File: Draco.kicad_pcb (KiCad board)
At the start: 2 copper layers, 114.3 x 44.5 mm, 122 parts, among them J1 Conn_01x03, J10 Conn_01x03, J11 Conn_01x06, J12 Conn_02x05_Odd_Even, J13 Conn_01x04, J14 Conn_01x01, J15 Micro_SD_Card, J16 Conn_01x03, J17 CHARGE_A, J18 CHARGE_C, J19 CHARGE_B, J2 Conn_01x03, J20 Conn_01x04, J3 Conn_01x03, J4 Conn_01x03, J5 Conn_01x03, J6 Conn_01x03, J7 Conn_01x03, J8 Conn_01x03, J9 Conn_01x03, Q1 BC817, Q2 Q_NMOS_DGS, Q3 BC817, Q4 Q_NMOS_DGS, Q5 BC817, Q6 Q_NMOS_DGS, U1 ATMEGA2560-16AU, U2 LOGIC-TXS0108EPWR(TSSOP20), U3 RFM95HW, U4 TPS54332, U5 TLV62568, U6 SAM-M8Q, U7 LSM9DS1TR‎, U8 MS5607, Y1 16MHz

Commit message: Added dragon
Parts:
- added G***: LOGO, Current_Control_Systems:Draco_Logo, B.Cu at (137.5, 98.3)
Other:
- board text added: "CHARGE_A"
- board text added: "CHARGE_B"
- board text added: "CHARGE_C"
- board text added: "VIN 8.4V"

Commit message: Starting design review
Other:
- board text added: "5V"
- board text added: "CAM"
- board text added: "CPU PWR"
- board text added: "DTR"
- board text added: "GND"
- board text added: "ISP"
- board text added: "MISO"
- board text added: "MOSI"
- board text added: "NC"
- board text added: "RX"
- board text added: "SERVO PWR"
- board text added: "TEST_STAND"
- board text added: "TX"
- board text added: "VIN"
- board text added: "VIN 6-22V"
- board text added: "~~ + -"
- board text removed: "VIN 8.4V"
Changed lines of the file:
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@@
     (links 323)
     (no_connects 4)
-    (area 76.124999 76.124999 190.575001 120.725001)
+    (area 67.524143 73.53518 199.252058 122.996953)
     (thickness 1.6)
-    (drawings 10)
+    (drawings 37)
     (tracks 1618)
     (zones 0)
@@
   (page A4)
   (layers
-    (0 F.Cu signal hide)
-    (31 B.Cu signal hide)
+    (0 F.Cu signal)
+    (31 B.Cu signal)
     (32 B.Adhes user)
     (33 F.Adhes user)
@@
     (41 Cmts.User user)
     (42 Eco1.User user)
-    (43 Eco2.User user hide)
+    (43 Eco2.User user)
     (44 Edge.Cuts user)
     (45 Margin user)
@@
   )
   (setup
-    (last_trace_width 0.16)
+    (last_trace_width 0.25)
     (user_trace_width 0.16)
     (user_trace_width 0.75)
@@
     (pad_to_mask_clearance 0.2)
     (aux_axis_origin 0 0)
-    (visible_elements 7FFFEDFF)
+    (visible_elements 7FFFEFFF)
     (pcbplotparams
       (layerselection 0x00030_80000001)
@@
     (descr "Through hole straight pin header, 1x03, 2.54mm pitch, single row")
     (tags "Through hole pin header THT 1x03 2.54mm single row")
-    (fp_text reference JP1 (at 0.0508 7.2644 180) (layer F.SilkS)
+    (fp_text reference JP1 (at 0.0508 7.2644) (layer F.SilkS) hide
       (effects (font (size 1 1) (thickness 0.15)))
     )
@@
     (descr "Through hole straight pin header, 1x02, 2.54mm pitch, single row")
     (tags "Through hole pin header THT 1x02 2.54mm single row")
-    (fp_text reference JP2 (at 0.0254 -2.1844) (layer F.SilkS)
+    (fp_text reference JP2 (at 0.0254 -2.1844) (layer F.SilkS) hide
       (effects (font (size 1 1) (thickness 0.15)))
     )
@@
       (xy -7.2136 3.7846)) (layer B.SilkS) (width 0.01))
   )
+  (gr_text TX (at 133.2738 79.9592) (layer F.SilkS)
+    (effects (font (size 0.5 0.5) (thickness 0.125)))
+  )
+  (gr_text RX (at 135.89 79.9338) (layer F.SilkS)
+    (effects (font (size 0.5 0.5) (thickness 0.125)))
+  )
+  (gr_text NC (at 141.0208 79.9592) (layer F.SilkS)
+    (effects (font (size 0.5 0.5) (thickness 0.125)))
+  )
+  (gr_text GND (at 143.5608 79.9846) (layer F.SilkS)
+    (effects (font (size 0.5 0.5) (thickness 0.125)))
+  )
+  (gr_text 5V (at 138.4554 79.9338) (layer F.SilkS)
+    (effects (font (size 0.5 0.5) (thickness 0.125)))
+  )
+  (gr_text DTR (at 130.7592 79.9592) (layer F.SilkS)
+    (effects (font (size 0.5 0.5) (thickness 0.125)))
+  )
+  (gr_line (start 108.9152 117.3226) (end 108.966 117.3226) (angle 90) (layer F.SilkS) (width 0.2))
+  (gr_line (start 108.9152 117.8814) (end 108.9152 117.3226) (angle 90) (layer F.SilkS) (width 0.2))
+  (gr_line (start 108.9152 111.2266) (end 108.9152 111.7346) (angle 90) (layer F.SilkS) (width 0.2))
+  (gr_line (start 108.9152 111.252) (end 109.1438 111.252) (angle 90) (layer F.SilkS) (width 0.2))
+  (gr_line (start 108.9152 114.2238) (end 109.093 114.2238) (angle 90) (layer F.SilkS) (width 0.2))
+  (gr_line (start 108.9152 113.7158) (end 108.9152 114.2238) (angle 90) (layer F.SilkS) (width 0.2))
+  (gr_line (start 108.9152 114.8842) (end 109.1184 114.8842) (angle 90) (layer F.SilkS) (width 0.2))
+  (gr_line (start 108.9152 115.3668) (end 108.9152 114.8842) (angle 90) (layer F.SilkS) (width 0.2))
+  (gr_line (start 108.9152 117.8814) (end 109.1184 117.8814) (angle 90) (layer F.SilkS) (width 0.2))
+  (gr_text 5V (at 108.8644 116.2812 90) (layer F.SilkS)
+    (effects (font (size 0.5 0.5) (thickness 0.125)))
+  )
+  (gr_text VIN (at 108.8898 112.6236 90) (layer F.SilkS)
+    (effects (font (size 0.5 0.5) (thickness 0.125)))
+  )
+  (gr_text "SERVO\nPWR" (at 110.744 119.4308) (layer F.SilkS)
+    (effects (font (size 0.5 0.5) (thickness 0.125)))
+  )
+  (gr_text "CPU\nPWR" (at 90.7796 102.2604) (layer F.SilkS)
+    (effects (font (size 1 1) (thickness 0.25)))
+  )
+  (gr_text ISP (at 118.4148 92.71) (layer F.SilkS)
+    (effects (font (size 1 1) (thickness 0.25)))
+  )
+  (gr_text GND (at 115.7478 77.4192) (layer F.SilkS)
+    (effects (font (size 0.5 0.5) (thickness 0.125)))
+  )
+  (gr_text "MISO\n" (at 121.2088 77.4446) (layer F.SilkS)
+    (effects (font (size 0.5 0.5) (thickness 0.125)))
+  )
+  (gr_text 5V (at 115.5954 91.3384) (layer F.SilkS)
+    (effects (font (size 0.5 0.5) (thickness 0.125)))
+  )
+  (gr_text MOSI (at 121.3104 91.313) (layer F.SilkS)
+    (effects (font (size 0.5 0.5) (thickness 0.125)))
+  )
+  (gr_text "~~ + -" (at 150.368 116.4844 270) (layer F.SilkS)
+    (effects (font (size 1.5 1.5) (thickness 0.3)))
+  )
+  (gr_text "CAM\n" (at 162.306 83.6168) (layer F.SilkS)
+    (effects (font (size 1 1) (thickness 0.25)))
+  )
+  (gr_text TEST_STAND (at 152.5016 83.6422) (layer F.SilkS)
+    (effects (font (size 1 1) (thickness 0.25)))
+  )
   (gr_text "CHARGE_B\n" (at 109.5248 76.962) (layer F.SilkS)
     (effects (font (size 1 1) (thickness 0.25)))
@@
     (effects (font (size 1 1) (thickness 0.25)))
   )
-  (gr_text "VIN 8.4V" (at 88.0618 110.8456 90) (layer F.SilkS)
+  (gr_text "VIN 6-22V" (at 88.0618 110.8456 90) (layer F.SilkS)
     (effects (font (size 0.5 0.5) (thickness 0.125)))
   )
@@
     (polygon
       (pts
-        (xy 76.2 120.6246) (xy 190.4746 120.6246) (xy 190.5 76.2) (xy 76.2 76.2254) (xy 76.2254 76.2254)
+        (xy 76.2 76.2254) (xy 76.2 120.6246) (xy 190.5254 120.65) (xy 190.4746 76.2254)
       )
     )

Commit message: Added camera resistor divider
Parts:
- added R38: 0, Resistors_SMD:R_0805, B.Cu at (164.3, 83.3)
- added R39: 0, Resistors_SMD:R_0805, B.Cu at (166.9, 83.3)
- added R40: 0, Resistors_SMD:R_0805, B.Cu at (169.3, 83.2)
- R2: value 1k -> 2k7
- R3: value 1k -> 4k7
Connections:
- net /~FIRE_A renamed /FIRE_A
- net /~FIRE_B renamed /FIRE_B
- net /~FIRE_C renamed /FIRE_C
- J11 pad 5: (no net) -> Net-(J11-Pad5)
- J12 pad 3: (no net) -> Net-(J12-Pad3)
- J15 pad 1: (no net) -> Net-(J15-Pad1)
- J15 pad 8: (no net) -> Net-(J15-Pad8)
- U1 pad 1: (no net) -> Net-(U1-Pad1)
- U1 pad 12: (no net) -> Net-(U1-Pad12)
- U1 pad 13: (no net) -> Net-(U1-Pad13)
- U1 pad 14: (no net) -> Net-(U1-Pad14)
- U1 pad 18: (no net) -> Net-(U1-Pad18)
- U1 pad 19: (no net) -> Net-(U1-Pad19)
- U1 pad 23: (no net) -> Net-(U1-Pad23)
- U1 pad 24: (no net) -> Net-(U1-Pad24)
- U1 pad 25: (no net) -> Net-(U1-Pad25)
- U1 pad 26: (no net) -> Net-(U1-Pad26)
- U1 pad 27: (no net) -> Net-(U1-Pad27)
- U1 pad 28: (no net) -> Net-(U1-Pad28)
- U1 pad 29: (no net) -> Net-(U1-Pad29)
- U1 pad 4: (no net) -> Net-(U1-Pad4)
- U1 pad 47: (no net) -> Net-(U1-Pad47)
- U1 pad 48: (no net) -> Net-(U1-Pad48)
- U1 pad 49: (no net) -> Net-(U1-Pad49)
- U1 pad 5: (no net) -> Net-(U1-Pad5)
- U1 pad 50: (no net) -> Net-(U1-Pad50)
- U1 pad 51: (no net) -> /SERVO9
- U1 pad 52: (no net) -> /SERVO10
- U1 pad 53: (no net) -> Net-(U1-Pad53)
- U1 pad 54: (no net) -> Net-(U1-Pad54)
- U1 pad 55: (no net) -> Net-(U1-Pad55)
- U1 pad 56: (no net) -> Net-(U1-Pad56)
- U1 pad 57: (no net) -> Net-(U1-Pad57)
- U1 pad 58: (no net) -> Net-(U1-Pad58)
- U1 pad 59: (no net) -> Net-(U1-Pad59)
- U1 pad 60: (no net) -> Net-(U1-Pad60)
- U1 pad 63: (no net) -> Net-(U1-Pad63)
- U1 pad 64: (no net) -> Net-(U1-Pad64)
- U1 pad 65: (no net) -> Net-(U1-Pad65)
- U1 pad 69: (no net) -> Net-(U1-Pad69)
- U1 pad 70: (no net) -> Net-(U1-Pad70)
- U1 pad 79: (no net) -> Net-(U1-Pad79)
- U1 pad 8: /SERVO10 -> Net-(U1-Pad8)
- U1 pad 84: (no net) -> Net-(U1-Pad84)
- U1 pad 85: (no net) -> Net-(U1-Pad85)
- U1 pad 86: (no net) -> Net-(U1-Pad86)
- U1 pad 9: /SERVO9 -> Net-(U1-Pad9)
- U1 pad 90: (no net) -> Net-(U1-Pad90)
- U1 pad 91: (no net) -> Net-(U1-Pad91)
- U3 pad 11: (no net) -> Net-(U3-Pad11)
- U3 pad 12: (no net) -> Net-(U3-Pad12)
- U3 pad 15: (no net) -> Net-(U3-Pad15)
- U3 pad 16: (no net) -> Net-(U3-Pad16)
- U3 pad 7: (no net) -> Net-(U3-Pad7)
- U4 pad 3: (no net) -> Net-(U4-Pad3)
- U6 pad 18: (no net) -> Net-(U6-Pad18)
- U6 pad 7: (no net) -> Net-(U6-Pad7)
- U6 pad 8: (no net) -> Net-(U6-Pad8)
- U7 pad 10: (no net) -> Net-(U7-Pad10)
- U7 pad 13: (no net) -> Net-(U7-Pad13)
- U7 pad 5: (no net) -> Net-(U7-Pad5)
- U7 pad 6: (no net) -> Net-(U7-Pad6)
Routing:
- net /SERVO10: track 33.3 -> 19.2 mm
- net /SERVO9: track 30.4 -> 18.7 mm
- net GND: track 570.1 -> 580.7 mm
- net Net-(J13-Pad3): track 3.34 -> 5.37 mm
- net Net-(J13-Pad2): track 3.10 -> 5.11 mm
- net Net-(J13-Pad1): track 2.86 -> 4.85 mm
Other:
- board text added: "DO NOT SHORT"
- board text added: "PWR"
- board text added: "VIN 6-15V"
- board text removed: "CPU PWR"
- board text removed: "VIN 6-22V"

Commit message: work review
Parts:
- removed G***: LOGO, Current_Control_Systems:Draco_Logo
- added R41: 10k, Resistors_SMD:R_0805, F.Cu at (155.1, 105.8)
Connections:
- U1 pad 54: Net-(U1-Pad54) -> /OE
- U2 pad 10: +3V3 -> /OE
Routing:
- net /OE: track 0.00 -> 21.2 mm, vias 0 -> 3
- net GND: track 580.7 -> 584.4 mm
- net +3V3: track 215.9 -> 216.8 mm

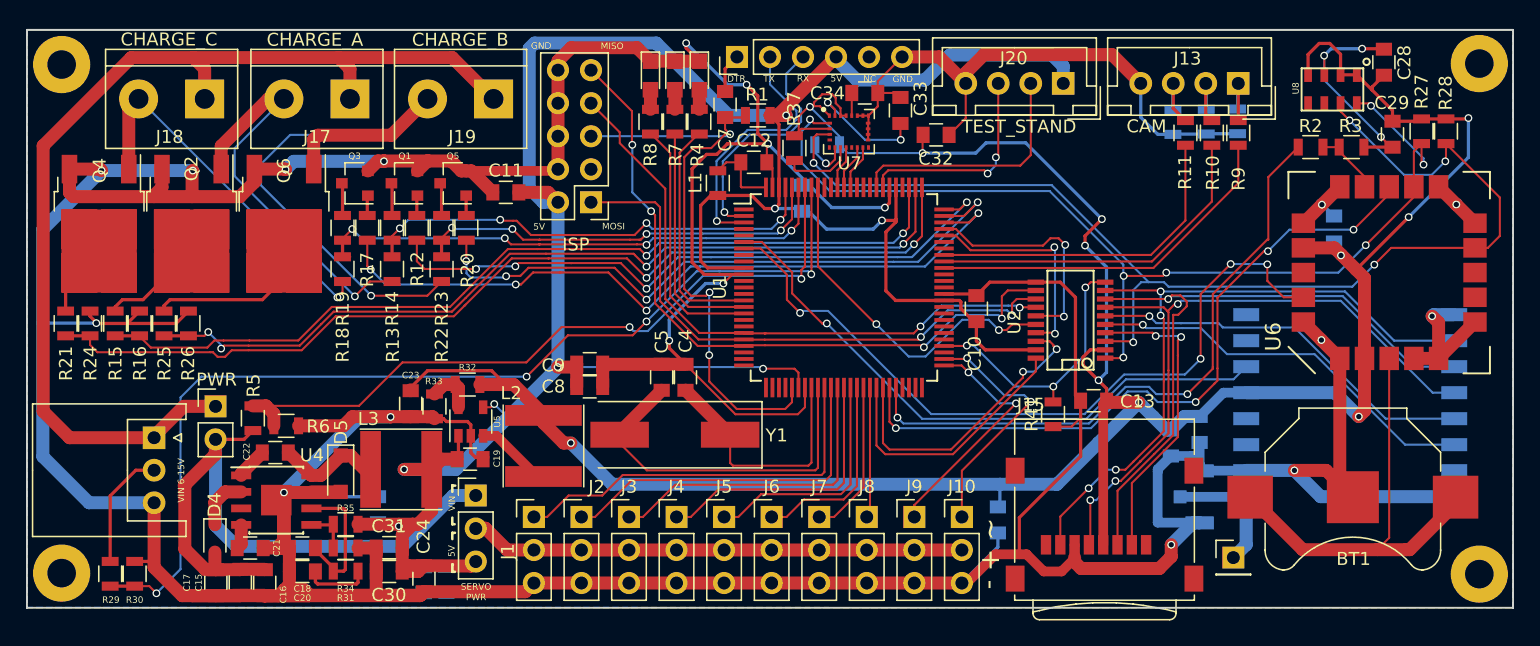
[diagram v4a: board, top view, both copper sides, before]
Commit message: Added camera power
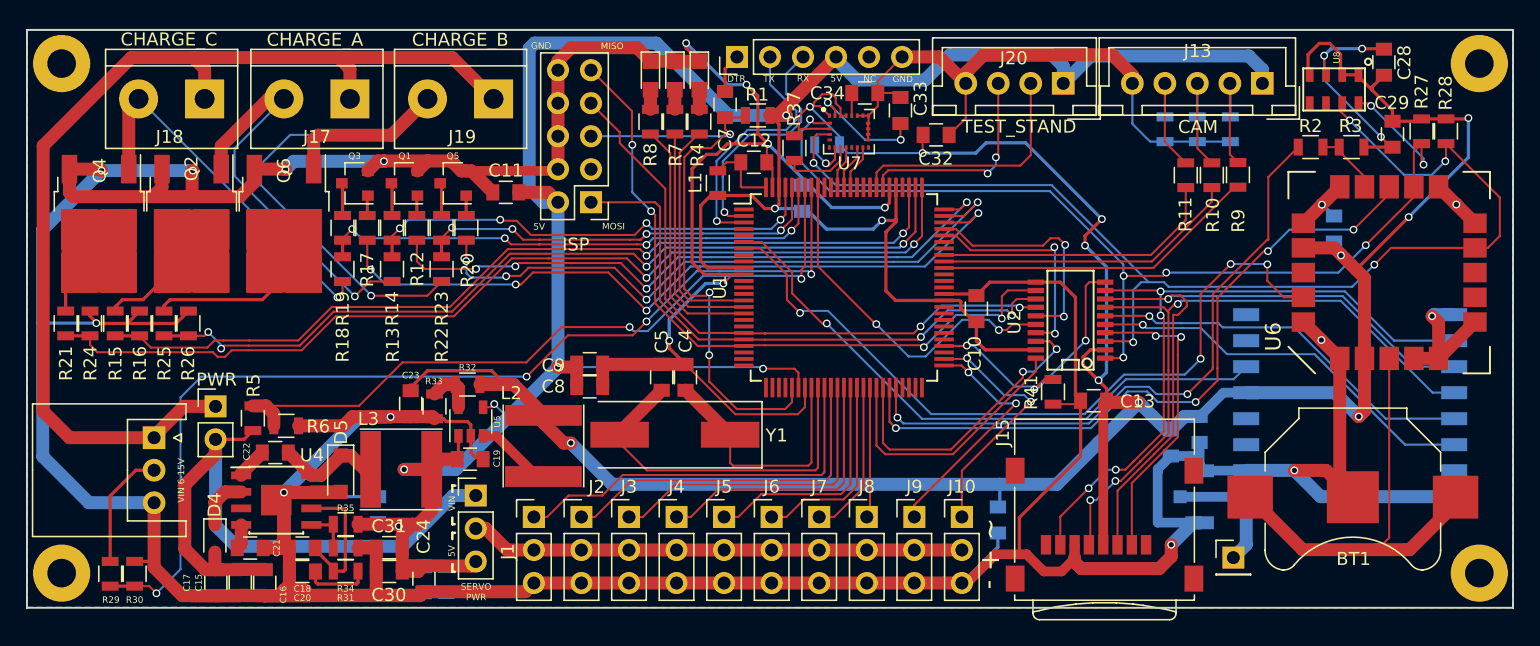
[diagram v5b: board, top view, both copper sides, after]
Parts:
- J13: value Conn_01x04 -> Conn_01x05; footprint Connectors_JST:JST_XH_B04B-XH-A_04x2.50mm_Straight -> Connectors_JST:JST_XH_B05B-XH-A_05x2.50mm_Straight
- R10: value 4.7K -> 2k7
- R11: value 0 -> 2k7
- R38, R39: value 0 -> 4k7
- moved R11 3.25 mm to (165.3, 87.4)
- moved R10 3.25 mm to (167.3, 87.4)
- moved R9 3.23 mm to (169.3, 87.4)
- moved J13 1.85 mm to (171.2, 80.3)
- moved R41 1.73 mm to (155.1, 104.0)
- moved R39 0.90 mm to (166.2, 83.8)
- moved R38 0.83 mm to (163.7, 83.8)
- moved R40 0.83 mm to (168.8, 83.8)
- moved U8 0.13 mm to (178.6, 79.7)
- moved MH1 0.08 mm to (78.9, 78.8)
- moved MH3 0.08 mm to (187.9, 118.0)
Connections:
- J13 pad 1: Net-(J13-Pad1) -> +5V
- J13 pad 4: GND -> Net-(J13-Pad4)
- R10 pad 1: Net-(J13-Pad2) -> Net-(J13-Pad3)
- R11 pad 1: Net-(J13-Pad3) -> Net-(J13-Pad4)
- R38 pad 2: Net-(J13-Pad3) -> Net-(J13-Pad4)
- R39 pad 2: Net-(J13-Pad2) -> Net-(J13-Pad3)
- R40 pad 2: Net-(J13-Pad1) -> Net-(J13-Pad2)
- R9 pad 1: Net-(J13-Pad1) -> Net-(J13-Pad2)
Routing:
- net +5V: track 215.6 -> 232.8 mm
- net Net-(J13-Pad4): track 0.00 -> 9.45 mm
- net Net-(J13-Pad1): track 4.85 -> 0.00 mm
- net Net-(J13-Pad2): track 5.11 -> 8.99 mm
- net Net-(J13-Pad3): track 5.37 -> 9.24 mm
- net /CAM_PHOTO: track 26.8 -> 23.6 mm
- net /CAM_PWR: track 25.4 -> 22.2 mm
- net /CAM_LED: track 28.2 -> 25.2 mm
- net GND: track 584.4 -> 582.7 mm
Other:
- board text added: "A14"
- board text added: "A15"
- board text added: "LED"
- board text added: "PHOTO"

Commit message: Added logo again because the dragon keeps dissapearing
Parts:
- added G***: LOGO, Current_Control_Systems:Draco_Logo, B.Cu at (138.6, 97.6)

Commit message: Figured out where the dragon goes
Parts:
- moved G*** 2.34 mm to (136.7, 98.9)
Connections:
- J11 pad 5: Net-(J11-Pad5) -> (no net)
- J12 pad 3: Net-(J12-Pad3) -> (no net)
- J15 pad 1: Net-(J15-Pad1) -> (no net)
- J15 pad 8: Net-(J15-Pad8) -> (no net)
- U1 pad 1: Net-(U1-Pad1) -> (no net)
- U1 pad 12: Net-(U1-Pad12) -> (no net)
- U1 pad 13: Net-(U1-Pad13) -> (no net)
- U1 pad 14: Net-(U1-Pad14) -> (no net)
- U1 pad 18: Net-(U1-Pad18) -> (no net)
- U1 pad 19: Net-(U1-Pad19) -> (no net)
- U1 pad 23: Net-(U1-Pad23) -> (no net)
- U1 pad 24: Net-(U1-Pad24) -> (no net)
- U1 pad 25: Net-(U1-Pad25) -> (no net)
- U1 pad 26: Net-(U1-Pad26) -> (no net)
- U1 pad 27: Net-(U1-Pad27) -> (no net)
- U1 pad 28: Net-(U1-Pad28) -> (no net)
- U1 pad 29: Net-(U1-Pad29) -> (no net)
- U1 pad 4: Net-(U1-Pad4) -> (no net)
- U1 pad 47: Net-(U1-Pad47) -> (no net)
- U1 pad 48: Net-(U1-Pad48) -> (no net)
- U1 pad 49: Net-(U1-Pad49) -> (no net)
- U1 pad 5: Net-(U1-Pad5) -> (no net)
- U1 pad 50: Net-(U1-Pad50) -> (no net)
- U1 pad 53: Net-(U1-Pad53) -> (no net)
- U1 pad 55: Net-(U1-Pad55) -> (no net)
- U1 pad 56: Net-(U1-Pad56) -> (no net)
- U1 pad 57: Net-(U1-Pad57) -> (no net)
- U1 pad 58: Net-(U1-Pad58) -> (no net)
- U1 pad 59: Net-(U1-Pad59) -> (no net)
- U1 pad 60: Net-(U1-Pad60) -> (no net)
- U1 pad 63: Net-(U1-Pad63) -> (no net)
- U1 pad 64: Net-(U1-Pad64) -> (no net)
- U1 pad 65: Net-(U1-Pad65) -> (no net)
- U1 pad 69: Net-(U1-Pad69) -> (no net)
- U1 pad 70: Net-(U1-Pad70) -> (no net)
- U1 pad 79: Net-(U1-Pad79) -> (no net)
- U1 pad 8: Net-(U1-Pad8) -> (no net)
- U1 pad 84: Net-(U1-Pad84) -> (no net)
- U1 pad 85: Net-(U1-Pad85) -> (no net)
- U1 pad 86: Net-(U1-Pad86) -> (no net)
- U1 pad 9: Net-(U1-Pad9) -> (no net)
- U1 pad 90: Net-(U1-Pad90) -> (no net)
- U1 pad 91: Net-(U1-Pad91) -> (no net)
- U3 pad 11: Net-(U3-Pad11) -> (no net)
- U3 pad 12: Net-(U3-Pad12) -> (no net)
- U3 pad 15: Net-(U3-Pad15) -> (no net)
- U3 pad 16: Net-(U3-Pad16) -> (no net)
- U3 pad 7: Net-(U3-Pad7) -> (no net)
- U4 pad 3: Net-(U4-Pad3) -> (no net)
- U6 pad 18: Net-(U6-Pad18) -> (no net)
- U6 pad 7: Net-(U6-Pad7) -> (no net)
- U6 pad 8: Net-(U6-Pad8) -> (no net)
- U7 pad 10: Net-(U7-Pad10) -> (no net)
- U7 pad 13: Net-(U7-Pad13) -> (no net)
- U7 pad 5: Net-(U7-Pad5) -> (no net)
- U7 pad 6: Net-(U7-Pad6) -> (no net)

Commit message: Added website
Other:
- board text added: "Draco_Rev1 Rocket Control Board By Vlad Pomogaev currentcontrolsystems.com"
- board text removed: "Draco_Rev1 Rocket Control Board By Vlad Pomogaev"
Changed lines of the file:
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@@
     (effects (font (size 0.5 0.5) (thickness 0.125)))
   )
-  (gr_text "Draco_Rev1\nRocket Control Board\nBy Vlad Pomogaev" (at 119.4816 109.093 270) (layer B.SilkS)
+  (gr_text "Draco_Rev1\nRocket Control Board\nBy Vlad Pomogaev\ncurrentcontrolsystems.com" (at 116.5606 109.1946 270) (layer B.SilkS)
     (effects (font (size 1 1) (thickness 0.25)) (justify left mirror))
   )
